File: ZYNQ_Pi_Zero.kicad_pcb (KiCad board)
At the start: 4 copper layers, 33 parts, among them Q501 2N7002, Q502 2N7002, Q503 2N7002, U101 xc7z010clg400, U201 MT41K256M16TW-107_P, U301 W25Q256FVEI, U501 TPD4E05U06DQA, U502 TPD4E05U06DQA

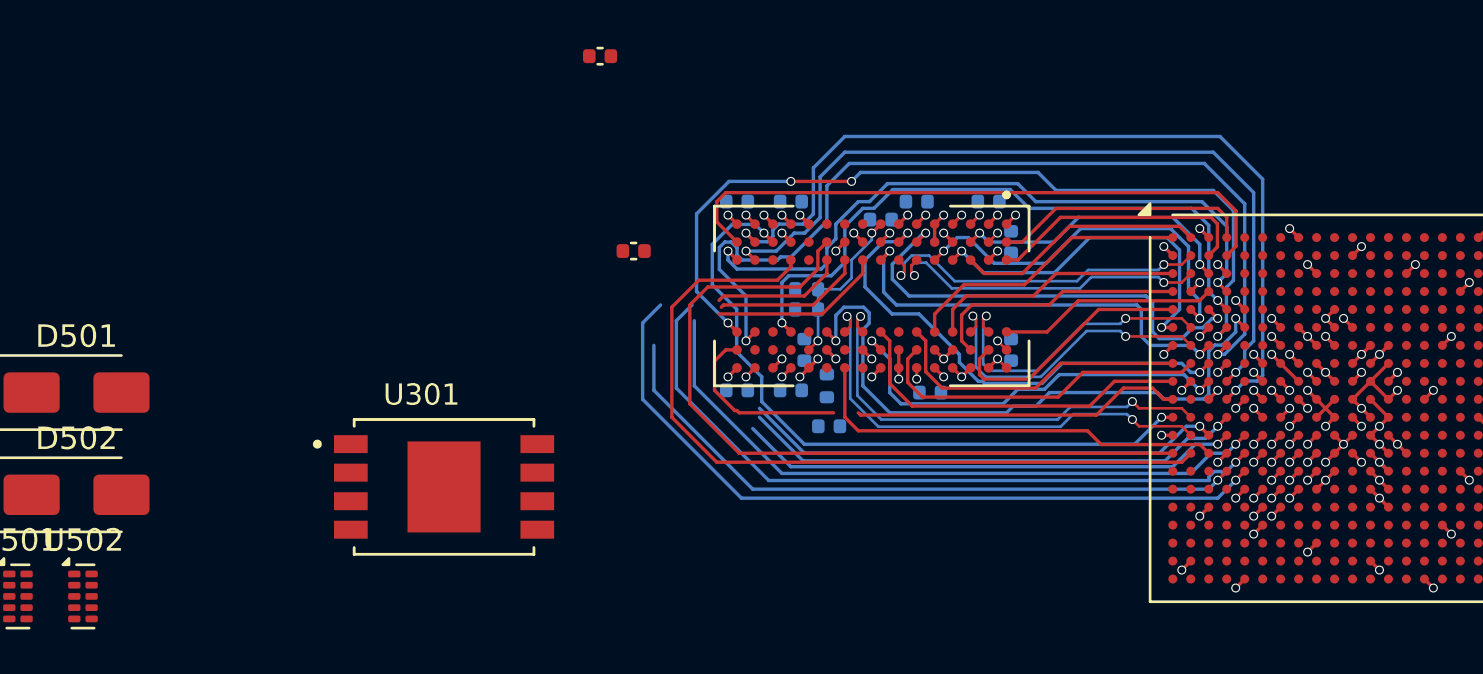
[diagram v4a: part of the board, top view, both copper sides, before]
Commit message: feat: continue routing ddr3
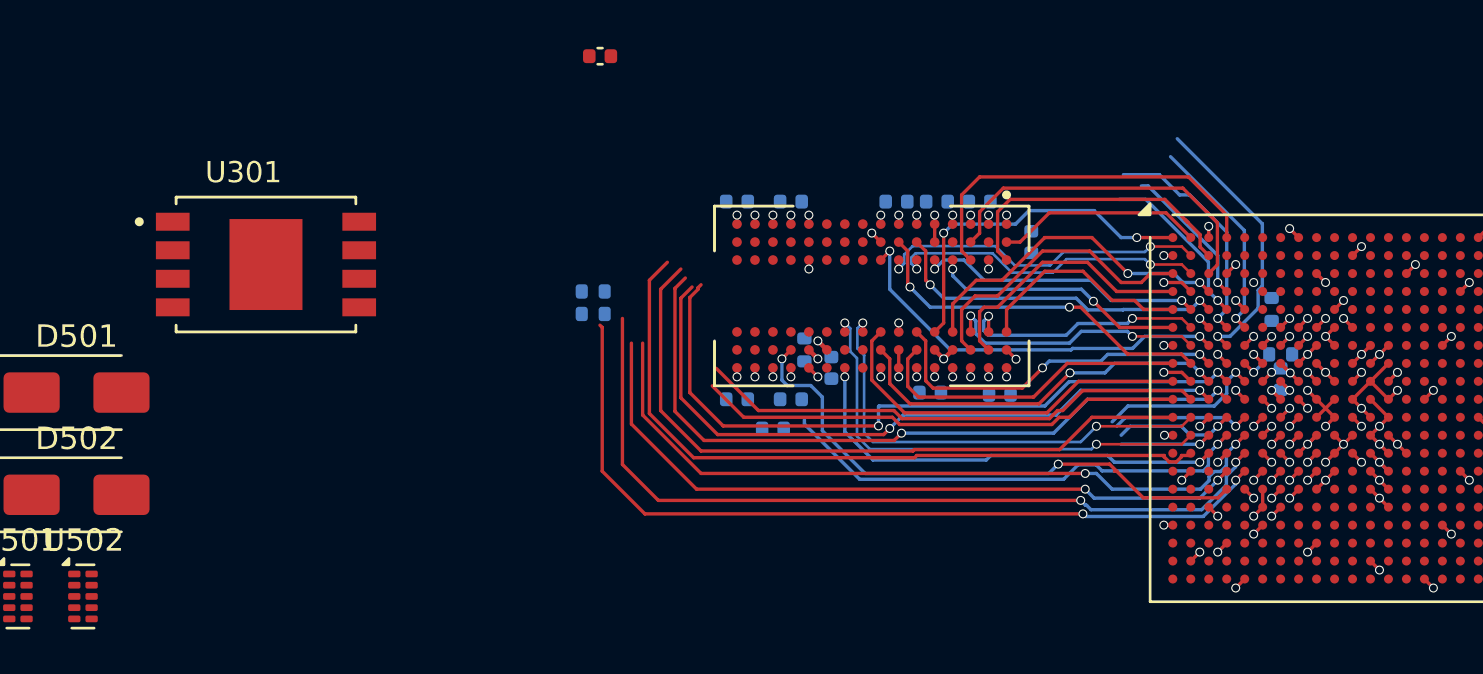
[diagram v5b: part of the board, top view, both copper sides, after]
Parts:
- added R204: 80R6, Resistor_SMD:R_0402_1005Metric, B.Cu at (145.8, 95.6)
- added R205: 80R6, Resistor_SMD:R_0402_1005Metric, B.Cu at (146.2, 97.6)
- C206: moved to B.Cu
- moved C208 21.2 mm to (146.2, 98.7)
- moved U301 12.7 mm to (101.0, 93.6)
- moved C206 10.2 mm to (126.2, 98.2), turned to -90 degrees
- moved R202 9.50 mm to (115.6, 95.8)
- moved R203 9.50 mm to (115.6, 94.8)
- moved C210 2.50 mm to (123.6, 100.9)
- moved C211 2.06 mm to (133.7, 99.4), turned to 0 degrees
- moved R201 1.89 mm to (125.0, 97.4)
- moved C205 1.06 mm to (129.1, 90.8)
- moved C202 0.90 mm to (130.9, 90.8), turned to 0 degrees
- moved C212 0.90 mm to (135.1, 92.6)
- moved C209 0.40 mm to (124.4, 99.6)
- moved C214 0.40 mm to (122.0, 99.6)
- moved C201 0.40 mm to (132.8, 90.8)
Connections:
- U201 pad A2: /DDR3/DDR_D3 -> /DDR3/DDR_D2
- U201 pad A7: /DDR3/DDR_D4 -> /DDR3/DDR_D7
- U201 pad B8: /DDR3/DDR_D7 -> /DDR3/DDR_D5
- U201 pad C3: /DDR3/DDR_D2 -> /DDR3/DDR_D3
- U201 pad C8: /DDR3/DDR_D5 -> /DDR3/DDR_D6
- U201 pad D7: /DDR3/DDR_D6 -> /DDR3/DDR_D4
- U201 pad F7: /DDR3/DDR_D14 -> /DDR3/DDR_D11
- U201 pad F8: /DDR3/DDR_D13 -> /DDR3/DDR_D14
- U201 pad G2: /DDR3/DDR_D11 -> /DDR3/DDR_D13
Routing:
- net /DDR3/DDR_~{CS}: track 34.5 -> 0.00 mm
- net /DDR3/DDR_A3: track 1.13 -> 30.3 mm
- net /DDR3/DDR_A11: track 40.6 -> 12.1 mm, vias 2 -> 1
- net /DDR3/DDR_~{RESET}: track 27.9 -> 0.00 mm
- net /DDR3/DDR_A14: track 37.8 -> 10.2 mm, vias 4 -> 1
- net /DDR3/DDR_BA1: track 0.00 -> 25.0 mm, vias 0 -> 2
- net /DDR3/DDR_A13: track 29.7 -> 6.45 mm, vias 2 -> 1
- net /DDR3/DDR_A1: track 0.00 -> 22.7 mm
- net /DDR3/DDR_A12: track 28.8 -> 7.59 mm, vias 2 -> 1
- net /DDR3/DDR_A10: track 27.9 -> 9.29 mm, vias 2 -> 1
- net /DDR3/DDR_A2: track 21.5 -> 4.07 mm
- net /DDR3/DDR_A6: track 22.4 -> 5.35 mm
- net /DDR3/DDR_BA2: track 0.00 -> 7.70 mm, vias 0 -> 2
- net /DDR3/DDR_A7: track 38.6 -> 32.3 mm
- net /DDR3/DDR_D11: track 22.2 -> 15.9 mm
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
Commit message: feat: continue routing ddr
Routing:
- net /DDR3/DDR_~{RESET}: track 0.00 -> 27.6 mm
- net /DDR3/DDR_A11: track 12.1 -> 27.9 mm
- net /DDR3/DDR_A10: track 9.29 -> 23.3 mm
- net /DDR3/DDR_~{WE}: track 32.8 -> 44.6 mm, vias 2 -> 3
- net /DDR3/DDR_A13: track 6.45 -> 18.0 mm
- net /DDR3/DDR_A14: track 10.2 -> 21.4 mm
- net /DDR3/DDR_A12: track 7.59 -> 17.5 mm
- net /DDR3/DDR_A0: track 32.4 -> 40.6 mm, vias 0 -> 2
- net /DDR3/DDR_~{CAS}: track 36.9 -> 43.9 mm, vias 2 -> 3
- net /DDR3/DDR_ODT: track 36.4 -> 42.2 mm, vias 2 -> 3
- net /DDR3/DDR_~{RAS}: track 32.0 -> 37.8 mm, vias 2 -> 3
- net /DDR3/DDR_A3: track 30.3 -> 35.7 mm, vias 2 -> 4
- net /DDR3/DDR_A5: track 30.8 -> 35.9 mm, vias 0 -> 2
- net /DDR3/DDR_A7: track 32.3 -> 36.0 mm, vias 2 -> 4
- net /DDR3/DDR_A9: track 31.2 -> 34.2 mm, vias 2 -> 4
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
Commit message: feat: continue routing ddr
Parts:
- moved C210 9.61 mm to (114.0, 100.5)
- moved C209 9.60 mm to (114.8, 99.3)
- moved C214 9.20 mm to (112.8, 99.3)
- moved R201 2.70 mm to (125.0, 100.1)
- moved C206 1.91 mm to (126.4, 100.1)
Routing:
- net /DDR3/DDR_~{CS}: track 0.57 -> 34.7 mm, vias 1 -> 2
- net /DDR3/DDR_A2: track 4.07 -> 32.3 mm, vias 1 -> 2
- net /DDR3/DDR_BA0: track 6.19 -> 30.4 mm, vias 1 -> 2
- net /DDR3/DDR_A14: track 21.4 -> 44.5 mm, vias 1 -> 2
- net /DDR3/DDR_A6: track 5.35 -> 27.8 mm, vias 1 -> 2
- net /DDR3/DDR_BA2: track 7.70 -> 29.5 mm
- net /DDR3/DDR_ODT: track 42.2 -> 56.2 mm, vias 3 -> 2
- net /DDR3/DDR_A11: track 27.9 -> 40.8 mm
- net /DDR3/DDR_A13: track 18.0 -> 29.8 mm, vias 1 -> 2
- net /DDR3/DDR_~{WE}: track 44.6 -> 56.2 mm, vias 3 -> 2
- net /DDR3/DDR_~{RAS}: track 37.8 -> 48.3 mm, vias 3 -> 2
- net /DDR3/DDR_A12: track 17.5 -> 27.4 mm, vias 1 -> 2
- net /DDR3/DDR_~{CAS}: track 43.9 -> 52.0 mm, vias 3 -> 2
- net /DDR3/DDR_A1: track 22.7 -> 28.4 mm
- net /DDR3/DDR_A10: track 23.3 -> 29.0 mm, vias 1 -> 2
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
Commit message: feat: continue routing ddr
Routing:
- net /DDR3/DDR_~{WE}: track 56.2 -> 1.47 mm, vias 2 -> 1
- net /DDR3/DDR_ODT: track 56.2 -> 3.23 mm, vias 2 -> 1
- net /DDR3/DDR_~{CAS}: track 52.0 -> 1.37 mm, vias 2 -> 1
- net /DDR3/DDR_~{RAS}: track 48.3 -> 1.31 mm, vias 2 -> 1
- net /DDR3/DDR_A14: track 44.5 -> 14.5 mm
- net /DDR3/DDR_~{CS}: track 34.7 -> 5.69 mm, vias 2 -> 0
- net /DDR3/DDR_A11: track 40.8 -> 13.3 mm, vias 1 -> 2
- net /DDR3/DDR_A0: track 40.8 -> 14.3 mm, vias 2 -> 0
- net /DDR3/DDR_A3: track 35.7 -> 11.4 mm, vias 4 -> 1
- net /DDR3/DDR_A7: track 36.0 -> 11.9 mm, vias 4 -> 2
- net /DDR3/DDR_A6: track 27.8 -> 4.35 mm
- net /DDR3/DDR_A5: track 36.0 -> 12.8 mm, vias 2 -> 0
- net /DDR3/DDR_A9: track 33.7 -> 11.2 mm, vias 4 -> 1
- net /DDR3/DDR_A2: track 32.3 -> 10.4 mm, vias 2 -> 1
- net /DDR3/DDR_A10: track 29.0 -> 8.30 mm
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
